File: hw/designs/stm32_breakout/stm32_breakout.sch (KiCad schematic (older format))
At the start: 20 parts, among them J1 USB_B_Micro, J2 Conn_01x10_Male, J3 Conn_01x10_Male, J4 Conn_01x03_Male, U1 AP7361C-33E, U2 STM32L031F6Px, U3 KC2016Z, Y1 ABS25-32.768KHZ-6-T

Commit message: Added KC2016 footprint
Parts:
- U3: footprint (none) -> Custom:KC2016Z
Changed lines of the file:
@@
 F 0 "U3" H 9294 2796 50  0000 L CNN
 F 1 "KC2016Z" H 9294 2705 50  0000 L CNN
-F 2 "" H 9000 2900 50  0001 C CNN
+F 2 "Custom:KC2016Z" H 9000 2900 50  0001 C CNN
 F 3 "https://global.kyocera.com/prdct/electro/product/pdf/clock_z_xz_e.pdf" H 9000 2900 50  0001 C CNN
 	1    8850 2750

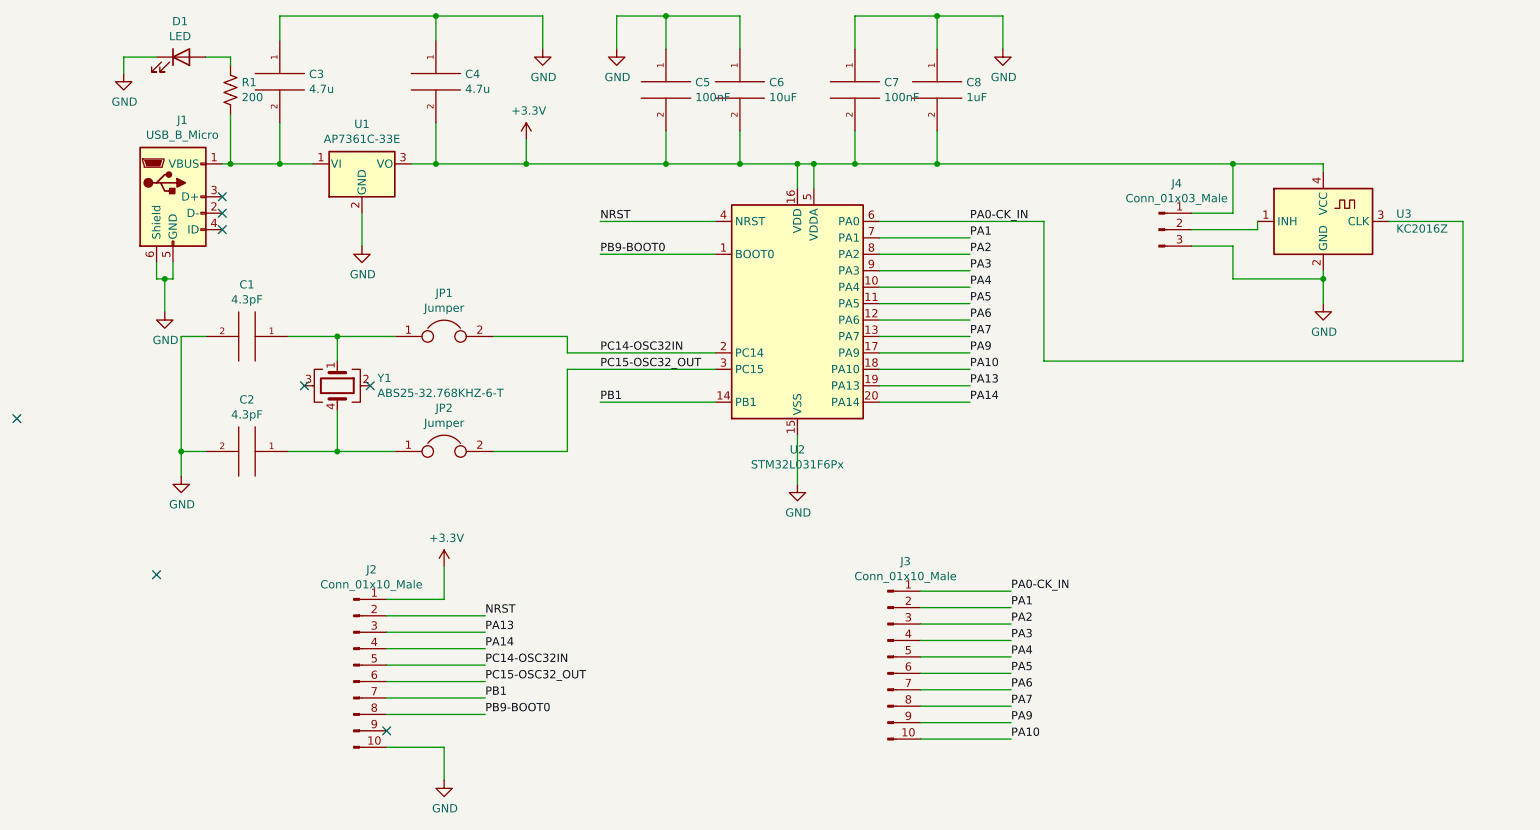
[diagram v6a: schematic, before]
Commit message: Removed RTC circuit. Changed pinout on headers. Updated jumpers to resistors instead. Started routing
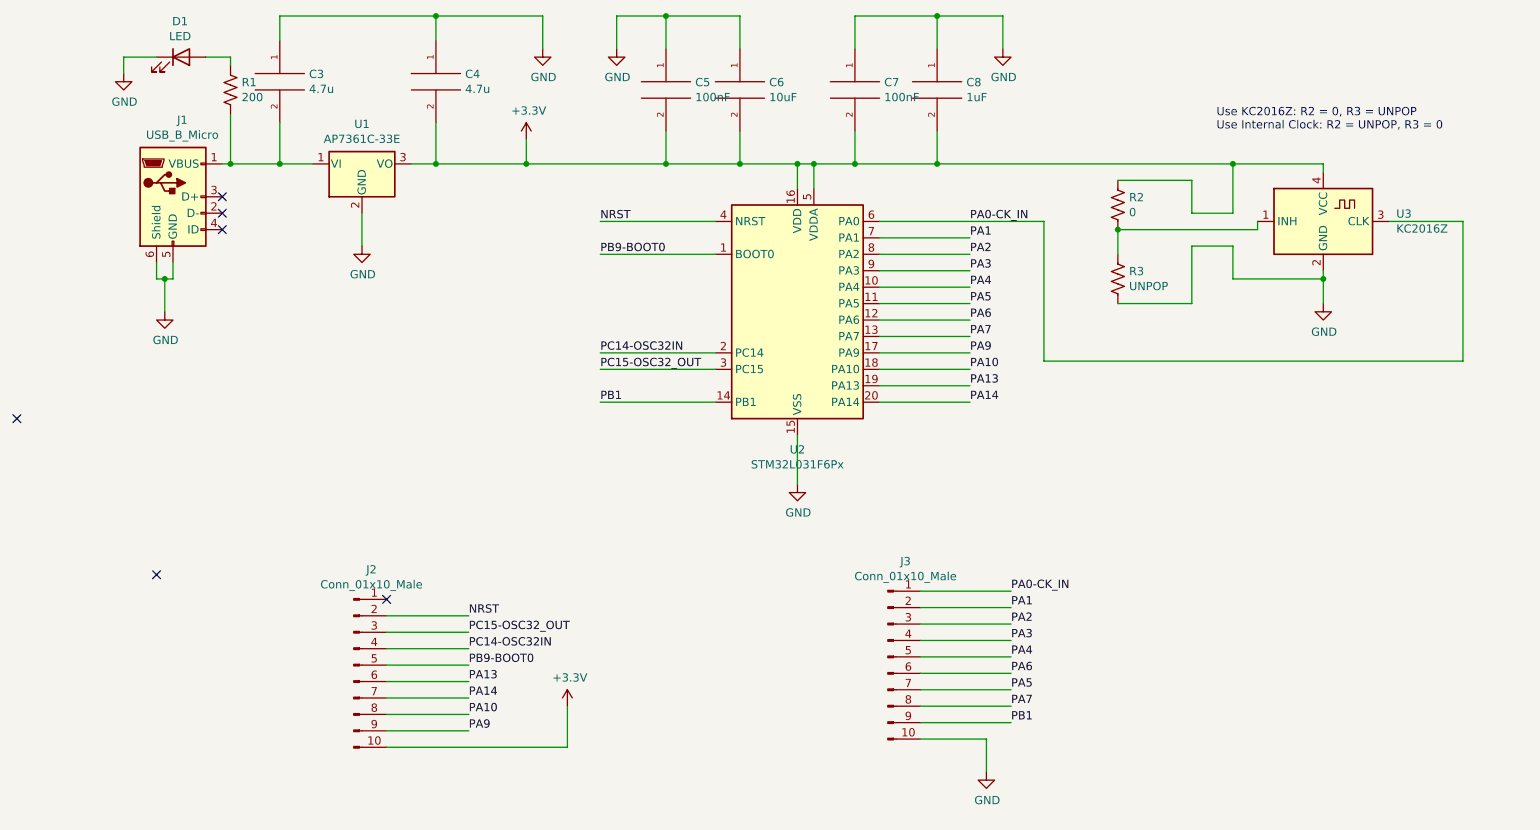
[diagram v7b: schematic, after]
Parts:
- removed C1, C2: 4.3pF, Capacitor_SMD:C_0805_2012Metric, symbol pspice:CAP
- removed J4: Conn_01x03_Male, Connector_PinSocket_2.54mm:PinSocket_1x03_P2.54mm_Vertical, symbol Connector:Conn_01x03_Male
- removed JP1, JP2: Jumper, Connector_PinSocket_2.54mm:PinSocket_1x02_P2.54mm_Vertical, symbol Device:Jumper
- removed Y1: ABS25-32.768KHZ-6-T, Custom:XTAL_ABS25-32.768KHZ-6-1-T, symbol Device:Crystal_GND23
- added R2: 0, Resistor_SMD:R_0805_2012Metric, symbol Device:R_US
- added R3: UNPOP, Resistor_SMD:R_0805_2012Metric, symbol Device:R_US
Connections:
- net +3V3: now also J2.10 (Pin_10), R2.1; no longer J2.1 (Pin_1)
- net GND: now also J3.10 (Pin_10), R3.2; no longer J2.10 (Pin_10)
- net PA10: now also J2.8 (Pin_8); no longer J3.10 (Pin_10)
- net PA13: now also J2.6 (Pin_6); no longer J2.3 (Pin_3)
- net PA14: now also J2.7 (Pin_7); no longer J2.4 (Pin_4)
- net PA5: now also J3.7 (Pin_7); no longer J3.6 (Pin_6)
- net PA6: now also J3.6 (Pin_6); no longer J3.7 (Pin_7)
- net PA9: now also J2.9 (Pin_9); no longer J3.9 (Pin_9)
- net PB1: now also J3.9 (Pin_9); no longer J2.7 (Pin_7)
- net PB9-BOOT0: now also J2.5 (Pin_5); no longer J2.8 (Pin_8)
- net PC14-OSC32IN: now also J2.4 (Pin_4); no longer J2.5 (Pin_5)
- net PC15-OSC32_OUT: now also J2.3 (Pin_3); no longer J2.6 (Pin_6)
- net at U3.1 (INH): now also R2.2, R3.1
- no-connect marks 8 -> 6
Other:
- note added: "Use KC2016Z: R2 = 0, R3 = UNPOP\nUse Internal Clock: R2 = UNPOP, R3 = 0"
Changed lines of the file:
@@
 Wire Wire Line
 	7150 3600 9700 3600
-$Comp
-L Connector:Conn_01x03_Male J4
-U 1 1 6083CA4A
-P 7850 2800
-F 0 "J4" H 7958 3081 50  0000 C CNN
-F 1 "Conn_01x03_Male" H 7958 2990 50  0000 C CNN
-F 2 "Connector_PinSocket_2.54mm:PinSocket_1x03_P2.54mm_Vertical" H 7850 2800 50  0001 C CNN
-F 3 "~" H 7850 2800 50  0001 C CNN
-	1    7850 2800
-	1    0    0    -1
-$EndComp
 Wire Wire Line
 	8050 2700 8300 2700
@@
 Wire Wire Line
 	8850 3100 8850 3250
-Wire Wire Line
-	8050 2800 8450 2800
 Wire Wire Line
 	8450 2800 8450 2750
 Text Label 4450 3650 0    50   ~ 0
 PC15-OSC32_OUT
-$Comp
-L Device:Crystal_GND23 Y1
-U 1 1 60849DF1
-P 2850 3750
-F 0 "Y1" V 2804 3994 50  0000 L CNN
-F 1 "ABS25-32.768KHZ-6-T" V 2895 3994 50  0000 L CNN
-F 2 "Custom:XTAL_ABS25-32.768KHZ-6-1-T" H 2850 3750 50  0001 C CNN
-F 3 "~" H 2850 3750 50  0001 C CNN
-	1    2850 3750
-	0    1    1    0
-$EndComp
-$Comp
-L pspice:CAP C1
-U 1 1 60862421
-P 2300 3450
-F 0 "C1" V 1985 3450 50  0000 C CNN
-F 1 "4.3pF" V 2076 3450 50  0000 C CNN
-F 2 "Capacitor_SMD:C_0805_2012Metric" H 2300 3450 50  0001 C CNN
-F 3 "~" H 2300 3450 50  0001 C CNN
-	1    2300 3450
-	0    1    1    0
-$EndComp
-$Comp
-L pspice:CAP C2
-U 1 1 608657C5
-P 2300 4150
-F 0 "C2" V 1985 4150 50  0000 C CNN
-F 1 "4.3pF" V 2076 4150 50  0000 C CNN
-F 2 "Capacitor_SMD:C_0805_2012Metric" H 2300 4150 50  0001 C CNN
-F 3 "~" H 2300 4150 50  0001 C CNN
-	1    2300 4150
-	0    1    1    0
-$EndComp
-Wire Wire Line
-	2850 3600 2850 3450
-Wire Wire Line
-	2850 3450 2550 3450
-Connection ~ 2850 3450
-Wire Wire Line
-	3200 4150 2850 4150
-Wire Wire Line
-	2850 4150 2850 3900
-Wire Wire Line
-	2850 4150 2550 4150
-Connection ~ 2850 4150
-Wire Wire Line
-	2050 3450 1900 3450
-Wire Wire Line
-	1900 3450 1900 4150
-Wire Wire Line
-	1900 4150 2050 4150
-Wire Wire Line
-	4250 4150 4250 3650
-$Comp
-L power:GND #PWR0107
-U 1 1 60879536
-P 1900 4300
-F 0 "#PWR0107" H 1900 4050 50  0001 C CNN
-F 1 "GND" H 1905 4127 50  0000 C CNN
-F 2 "" H 1900 4300 50  0001 C CNN
-F 3 "" H 1900 4300 50  0001 C CNN
-	1    1900 4300
-	1    0    0    -1
-$EndComp
-Wire Wire Line
-	1900 4150 1900 4300
-Connection ~ 1900 4150
 $Comp
 L Connector:Conn_01x10_Male J3
@@
 Text Label 6950 5300 0    50   ~ 0
 PA3
-Text Label 6950 5400 0    50   ~ 0
-PA4
-Text Label 6950 5500 0    50   ~ 0
-PA5
-Text Label 6950 5600 0    50   ~ 0
-PA6
 Text Label 6950 5700 0    50   ~ 0
 PA7
+Text Label 3650 5850 0    50   ~ 0
+PA9
+Text Label 3650 5550 0    50   ~ 0
+PA13
+Text Label 3650 5650 0    50   ~ 0
+PA14
+Wire Wire Line
+	6400 5100 6950 5100
+Wire Wire Line
+	6400 5200 6950 5200
+Wire Wire Line
+	6400 5300 6950 5300
+Wire Wire Line
+	6400 5700 6950 5700
+Text Label 3650 5350 0    50   ~ 0
+PC14-OSC32IN
 Text Label 6950 5800 0    50   ~ 0
-PA9
-Text Label 6950 5900 0    50   ~ 0
-PA10
-Text Label 3750 5250 0    50   ~ 0
-PA13
-Text Label 3750 5350 0    50   ~ 0
-PA14
-Wire Wire Line
-	6400 5100 6950 5100
-Wire Wire Line
-	6400 5200 6950 5200
-Wire Wire Line
-	6400 5300 6950 5300
-Wire Wire Line
-	6400 5400 6950 5400
-Wire Wire Line
-	6400 5500 6950 5500
-Wire Wire Line
-	6400 5600 6950 5600
-Wire Wire Line
-	6400 5700 6950 5700
-Wire Wire Line
-	6400 5800 6950 5800
-Wire Wire Line
-	6400 5900 6950 5900
-Wire Wire Line
-	3150 5250 3750 5250
-Wire Wire Line
-	3150 5350 3750 5350
-Text Label 3750 5450 0    50   ~ 0
-PC14-OSC32IN
-Text Label 3750 5650 0    50   ~ 0
 PB1
-Text Label 3750 5750 0    50   ~ 0
+Text Label 3650 5450 0    50   ~ 0
 PB9-BOOT0
-Text Label 3750 5550 0    50   ~ 0
+Text Label 3650 5250 0    50   ~ 0
 PC15-OSC32_OUT
-Wire Wire Line
-	3150 5450 3750 5450
-Wire Wire Line
-	3150 5550 3750 5550
-Wire Wire Line
-	3150 5650 3750 5650
-Wire Wire Line
-	3150 5750 3750 5750
 $Comp
 L power:+3.3V #PWR0108
@@
 L power:+3.3V #PWR0109
 U 1 1 6090C2FF
-P 3500 4850
-F 0 "#PWR0109" H 3500 4700 50  0001 C CNN
-F 1 "+3.3V" H 3515 5023 50  0000 C CNN
-F 2 "" H 3500 4850 50  0001 C CNN
-F 3 "" H 3500 4850 50  0001 C CNN
-	1    3500 4850
-	1    0    0    -1
-$EndComp
-Wire Wire Line
-	3500 4850 3500 5050
-Wire Wire Line
-	3500 5050 3150 5050
-Text Label 3750 5150 0    50   ~ 0
+P 4250 5700
+F 0 "#PWR0109" H 4250 5550 50  0001 C CNN
+F 1 "+3.3V" H 4265 5873 50  0000 C CNN
+F 2 "" H 4250 5700 50  0001 C CNN
+F 3 "" H 4250 5700 50  0001 C CNN
+	1    4250 5700
+	1    0    0    -1
+$EndComp
+Text Label 3650 5150 0    50   ~ 0
 NRST
-Wire Wire Line
-	3750 5150 3150 5150
-Wire Wire Line
-	3500 5950 3150 5950
 $Comp
 L power:GND #PWR0110
 U 1 1 6091C1DA
-P 3500 6150
-F 0 "#PWR0110" H 3500 5900 50  0001 C CNN
-F 1 "GND" H 3505 5977 50  0000 C CNN
-F 2 "" H 3500 6150 50  0001 C CNN
-F 3 "" H 3500 6150 50  0001 C CNN
-	1    3500 6150
-	1    0    0    -1
-$EndComp
-Wire Wire Line
-	3500 5950 3500 6150
+P 6800 6100
+F 0 "#PWR0110" H 6800 5850 50  0001 C CNN
+F 1 "GND" H 6805 5927 50  0000 C CNN
+F 2 "" H 6800 6100 50  0001 C CNN
+F 3 "" H 6800 6100 50  0001 C CNN
+	1    6800 6100
+	1    0    0    -1
+$EndComp
+Wire Wire Line
+	6800 5900 6800 6100
 Wire Wire Line
 	6400 5000 6950 5000
-$Comp
-L Device:Jumper JP2
-U 1 1 60875E00
-P 3500 4150
-F 0 "JP2" H 3500 4414 50  0000 C CNN
-F 1 "Jumper" H 3500 4323 50  0000 C CNN
-F 2 "Connector_PinSocket_2.54mm:PinSocket_1x02_P2.54mm_Vertical" H 3500 4150 50  0001 C CNN
-F 3 "~" H 3500 4150 50  0001 C CNN
-	1    3500 4150
-	1    0    0    -1
-$EndComp
 $Comp
 L MCU_ST_STM32L0:STM32L031F6Px U2
@@
 $EndComp
 Wire Wire Line
-	4250 4150 3800 4150
-Wire Wire Line
 	6150 2750 7150 2750
 Wire Wire Line
@@
 Wire Wire Line
 	6150 2850 6700 2850
-Wire Wire Line
-	3200 3450 2850 3450
-$Comp
-L Device:Jumper JP1
-U 1 1 60861856
-P 3500 3450
-F 0 "JP1" H 3500 3714 50  0000 C CNN
-F 1 "Jumper" H 3500 3623 50  0000 C CNN
-F 2 "Connector_PinSocket_2.54mm:PinSocket_1x02_P2.54mm_Vertical" H 3500 3450 50  0001 C CNN
-F 3 "~" H 3500 3450 50  0001 C CNN
-	1    3500 3450
-	1    0    0    -1
-$EndComp
 Text Label 4450 3550 0    50   ~ 0
 PC14-OSC32IN
 Wire Wire Line
 	4450 2950 5150 2950
-Wire Wire Line
-	4250 3650 5150 3650
-Wire Wire Line
-	3800 3450 4250 3450
-Wire Wire Line
-	5150 3550 4250 3550
-Wire Wire Line
-	4250 3550 4250 3450
 Wire Wire Line
 	4450 3850 5150 3850
@@
 NoConn ~ 900  3950
 NoConn ~ 1750 4900
-NoConn ~ 3150 5850
 NoConn ~ 2150 2600
 NoConn ~ 2150 2700
 NoConn ~ 2150 2800
-NoConn ~ 2650 3750
-NoConn ~ 3050 3750
+Wire Wire Line
+	3150 5950 4250 5950
+Wire Wire Line
+	4250 5700 4250 5950
+Wire Wire Line
+	6400 5600 6950 5600
+Wire Wire Line
+	6400 5400 6950 5400
+Text Label 6950 5600 0    50   ~ 0
+PA5
+Text Label 6950 5400 0    50   ~ 0
+PA4
+Wire Wire Line
+	6400 5500 6950 5500
+Text Label 6950 5500 0    50   ~ 0
+PA6
+Wire Wire Line
+	6400 5800 6950 5800
+Wire Wire Line
+	6400 5900 6800 5900
+Wire Wire Line
+	3150 5850 3650 5850
+Wire Wire Line
+	3150 5750 3650 5750
+Wire Wire Line
+	3150 5650 3650 5650
+Wire Wire Line
+	3150 5550 3650 5550
+Wire Wire Line
+	3150 5450 3650 5450
+Wire Wire Line
+	3150 5350 3650 5350
+Wire Wire Line
+	3150 5250 3650 5250
+Wire Wire Line
+	3650 5150 3150 5150
+NoConn ~ 3150 5050
+Text Label 3650 5750 0    50   ~ 0
+PA10
+Wire Wire Line
+	5150 3550 4450 3550
+Wire Wire Line
+	5150 3650 4450 3650
+$Comp
+L Device:R_US R2
+U 1 1 60D02F65
+P 7600 2650
+F 0 "R2" H 7668 2696 50  0000 L CNN
+F 1 "0" H 7668 2605 50  0000 L CNN
+F 2 "Resistor_SMD:R_0805_2012Metric" V 7640 2640 50  0001 C CNN
+F 3 "~" H 7600 2650 50  0001 C CNN
+	1    7600 2650
+	1    0    0    -1
+$EndComp
+$Comp
+L Device:R_US R3
+U 1 1 60D10526
+P 7600 3100
+F 0 "R3" H 7668 3146 50  0000 L CNN
+F 1 "UNPOP" H 7668 3055 50  0000 L CNN
+F 2 "Resistor_SMD:R_0805_2012Metric" V 7640 3090 50  0001 C CNN
+F 3 "~" H 7600 3100 50  0001 C CNN
+	1    7600 3100
+	1    0    0    -1
+$EndComp
+Wire Wire Line
+	8050 2700 8050 2500
+Wire Wire Line
+	8050 2500 7600 2500
+Wire Wire Line
+	7600 2800 7600 2950
+Wire Wire Line
+	7600 2800 8450 2800
+Connection ~ 7600 2800
+Wire Wire Line
+	7600 3250 8050 3250
+Wire Wire Line
+	8050 3250 8050 2900
+Text Notes 8200 2200 0    50   ~ 0
+Use KC2016Z: R2 = 0, R3 = UNPOP\nUse Internal Clock: R2 = UNPOP, R3 = 0
 $EndSCHEMATC

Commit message: Just pushing in case some changes didn't make it in
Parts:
- renumbered C3 to C1, C4 to C2, C5 to C3, C6 to C4, C7 to C5, C8 to C6
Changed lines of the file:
@@
 PA14
 $Comp
-L power:GND #PWR0101
+L power:GND #PWR08
 U 1 1 607E9570
 P 5650 4350
-F 0 "#PWR0101" H 5650 4100 50  0001 C CNN
+F 0 "#PWR08" H 5650 4100 50  0001 C CNN
 F 1 "GND" H 5655 4177 50  0000 C CNN
 F 2 "" H 5650 4350 50  0001 C CNN
@@
 	5650 4050 5650 4350
 $Comp
-L pspice:CAP C5
+L pspice:CAP C3
 U 1 1 607E9DE9
 P 4850 1950
-F 0 "C5" H 5028 1996 50  0000 L CNN
+F 0 "C3" H 5028 1996 50  0000 L CNN
 F 1 "100nF" H 5028 1905 50  0000 L CNN
 F 2 "Capacitor_SMD:C_0805_2012Metric" H 4850 1950 50  0001 C CNN
@@
 $EndComp
 $Comp
-L pspice:CAP C7
+L pspice:CAP C5
 U 1 1 607ECA39
 P 6000 1950
-F 0 "C7" H 6178 1996 50  0000 L CNN
+F 0 "C5" H 6178 1996 50  0000 L CNN
 F 1 "100nF" H 6178 1905 50  0000 L CNN
 F 2 "Capacitor_SMD:C_0805_2012Metric" H 6000 1950 50  0001 C CNN
@@
 $EndComp
 $Comp
-L pspice:CAP C8
+L pspice:CAP C6
 U 1 1 607ECE2C
 P 6500 1950
-F 0 "C8" H 6678 1996 50  0000 L CNN
+F 0 "C6" H 6678 1996 50  0000 L CNN
 F 1 "1uF" H 6678 1905 50  0000 L CNN
 F 2 "Capacitor_SMD:C_0805_2012Metric" H 6500 1950 50  0001 C CNN
@@
 	4550 1500 4850 1500
 $Comp
-L power:GND #PWR0102
+L power:GND #PWR010
 U 1 1 607FBD40
 P 6900 1700
-F 0 "#PWR0102" H 6900 1450 50  0001 C CNN
+F 0 "#PWR010" H 6900 1450 50  0001 C CNN
 F 1 "GND" H 6905 1527 50  0000 C CNN
 F 2 "" H 6900 1700 50  0001 C CNN
@@
 	6500 1500 6000 1500
 $Comp
-L power:GND #PWR0103
+L power:GND #PWR07
 U 1 1 60806A08
 P 4550 1700
-F 0 "#PWR0103" H 4550 1450 50  0001 C CNN
+F 0 "#PWR07" H 4550 1450 50  0001 C CNN
 F 1 "GND" H 4555 1527 50  0000 C CNN
 F 2 "" H 4550 1700 50  0001 C CNN
@@
 Connection ~ 5650 2400
 $Comp
-L pspice:CAP C6
+L pspice:CAP C4
 U 1 1 607EC639
 P 5300 1950
-F 0 "C6" H 5478 1996 50  0000 L CNN
+F 0 "C4" H 5478 1996 50  0000 L CNN
 F 1 "10uF" H 5478 1905 50  0000 L CNN
 F 2 "Capacitor_SMD:C_0805_2012Metric" H 5300 1950 50  0001 C CNN
@@
 	5650 2400 5650 2550
 $Comp
-L power:GND #PWR0104
+L power:GND #PWR03
 U 1 1 60812C1A
 P 3000 2900
-F 0 "#PWR0104" H 3000 2650 50  0001 C CNN
+F 0 "#PWR03" H 3000 2650 50  0001 C CNN
 F 1 "GND" H 3005 2727 50  0000 C CNN
 F 2 "" H 3000 2900 50  0001 C CNN
@@
 $EndComp
 $Comp
-L power:GND #PWR0105
+L power:GND #PWR02
 U 1 1 60817F53
 P 1800 3300
-F 0 "#PWR0105" H 1800 3050 50  0001 C CNN
+F 0 "#PWR02" H 1800 3050 50  0001 C CNN
 F 1 "GND" H 1805 3127 50  0000 C CNN
 F 2 "" H 1800 3300 50  0001 C CNN
@@
 	8850 3050 8850 3100
 $Comp
-L power:GND #PWR0106
+L power:GND #PWR011
 U 1 1 6082D318
 P 8850 3250
-F 0 "#PWR0106" H 8850 3000 50  0001 C CNN
+F 0 "#PWR011" H 8850 3000 50  0001 C CNN
 F 1 "GND" H 8855 3077 50  0000 C CNN
 F 2 "" H 8850 3250 50  0001 C CNN
@@
 PC15-OSC32_OUT
 $Comp
-L power:+3.3V #PWR0108
+L power:+3.3V #PWR04
 U 1 1 60904649
 P 4000 2250
-F 0 "#PWR0108" H 4000 2100 50  0001 C CNN
+F 0 "#PWR04" H 4000 2100 50  0001 C CNN
 F 1 "+3.3V" H 4015 2423 50  0000 C CNN
 F 2 "" H 4000 2250 50  0001 C CNN
@@
 	4000 2400 4850 2400
 $Comp
-L power:+3.3V #PWR0109
+L power:+3.3V #PWR06
 U 1 1 6090C2FF
 P 4250 5700
-F 0 "#PWR0109" H 4250 5550 50  0001 C CNN
+F 0 "#PWR06" H 4250 5550 50  0001 C CNN
 F 1 "+3.3V" H 4265 5873 50  0000 C CNN
 F 2 "" H 4250 5700 50  0001 C CNN
@@
 NRST
 $Comp
-L power:GND #PWR0110
+L power:GND #PWR09
 U 1 1 6091C1DA
 P 6800 6100
-F 0 "#PWR0110" H 6800 5850 50  0001 C CNN
+F 0 "#PWR09" H 6800 5850 50  0001 C CNN
 F 1 "GND" H 6805 5927 50  0000 C CNN
 F 2 "" H 6800 6100 50  0001 C CNN
@@
 	5150 2750 4450 2750
 $Comp
-L pspice:C C3
+L pspice:C C1
 U 1 1 60868E65
 P 2500 1900
-F 0 "C3" H 2678 1946 50  0000 L CNN
+F 0 "C1" H 2678 1946 50  0000 L CNN
 F 1 "4.7u" H 2678 1855 50  0000 L CNN
 F 2 "Capacitor_SMD:C_0805_2012Metric" H 2500 1900 50  0001 C CNN
@@
 $EndComp
 $Comp
-L pspice:CAP C4
+L pspice:CAP C2
 U 1 1 608699C3
 P 3450 1900
-F 0 "C4" H 3628 1946 50  0000 L CNN
+F 0 "C2" H 3628 1946 50  0000 L CNN
 F 1 "4.7u" H 3628 1855 50  0000 L CNN
 F 2 "Capacitor_SMD:C_0805_2012Metric" H 3450 1900 50  0001 C CNN
@@
 	2500 1650 2500 1500
 $Comp
-L power:GND #PWR0111
+L power:GND #PWR05
 U 1 1 608998B1
 P 4100 1700
-F 0 "#PWR0111" H 4100 1450 50  0001 C CNN
+F 0 "#PWR05" H 4100 1450 50  0001 C CNN
 F 1 "GND" H 4105 1527 50  0000 C CNN
 F 2 "" H 4100 1700 50  0001 C CNN
